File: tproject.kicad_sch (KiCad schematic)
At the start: 28 parts, among them J1 USB_B_Micro, J2 Conn_01x04_Pin, J3 Conn_01x04_Pin, J4 Conn_01x04_Pin, SW1 SW_SPDT, U1 STM32F103C8T6, U2 AMS1117-3.3, Y1 16MHz

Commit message: Replace SW1 with SMD PCM12 footprint, add Wurth USB STEP model, and add design note 0011
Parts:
- SW1: footprint Button_Switch_THT:SW_E-Switch_EG1224_SPDT_Angled -> Button_Switch_SMD:SW_SPDT_PCM12
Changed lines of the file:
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@@
 			)
 		)
-		(property "Footprint" "Button_Switch_THT:SW_E-Switch_EG1224_SPDT_Angled"
+		(property "Footprint" "Button_Switch_SMD:SW_SPDT_PCM12"
 			(at 149.86 62.23 0)
 			(effects

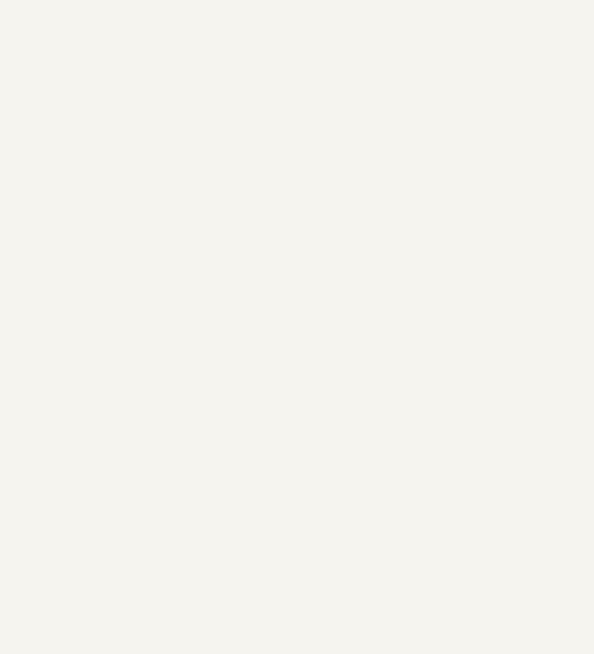
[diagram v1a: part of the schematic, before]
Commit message: Add board outline (38.54x33.17mm), 4x M2 mounting holes, adjust 8 components and add design note 0014
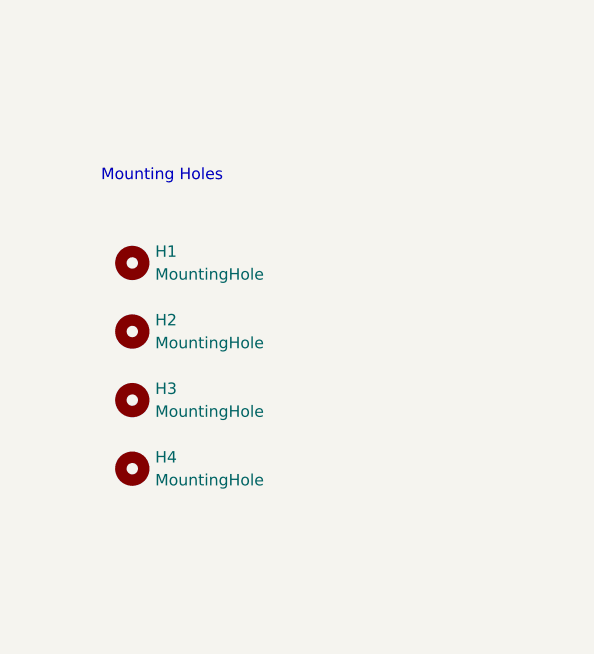
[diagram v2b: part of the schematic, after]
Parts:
- added H1, H2, H3, H4: MountingHole, MountingHole:MountingHole_2.2mm_M2, symbol Mechanical:MountingHole
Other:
- note added: "Mounting Holes"

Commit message: Fix Conn_01x04 footprint: 1.00mm SMD → 2.54mm through-hole (J2, J3, J4)
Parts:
- J2, J3, J4: footprint Connector_PinHeader_1.00mm:PinHeader_1x04_P1.00mm_Vertical_SMD_Pin1Right -> Connector_PinHeader_2.54mm:PinHeader_1x04_P2.54mm_Vertical
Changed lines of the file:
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@@
 			)
 		)
-		(property "Footprint" "Connector_PinHeader_1.00mm:PinHeader_1x04_P1.00mm_Vertical_SMD_Pin1Right"
+		(property "Footprint" "Connector_PinHeader_2.54mm:PinHeader_1x04_P2.54mm_Vertical"
 			(at 236.22 111.76 0)
 			(effects
@@
 			)
 		)
-		(property "Footprint" "Connector_PinHeader_1.00mm:PinHeader_1x04_P1.00mm_Vertical_SMD_Pin1Right"
+		(property "Footprint" "Connector_PinHeader_2.54mm:PinHeader_1x04_P2.54mm_Vertical"
 			(at 124.46 137.16 0)
 			(effects
@@
 			)
 		)
-		(property "Footprint" "Connector_PinHeader_1.00mm:PinHeader_1x04_P1.00mm_Vertical_SMD_Pin1Right"
+		(property "Footprint" "Connector_PinHeader_2.54mm:PinHeader_1x04_P2.54mm_Vertical"
 			(at 124.46 109.22 0)
 			(effects

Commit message: update with prompt result @usb-hub-sch-01-power~
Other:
- added sheet USB Hub (tproject-hub.kicad_sch)
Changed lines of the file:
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@@
+		)
+	)
+	(sheet
+		(at 20 160)
+		(size 30 15)
+		(fields_autoplaced yes)
+		(stroke
+			(width 0.152)
+			(type default)
+		)
+		(fill
+			(color 0 0 0 0.0000)
+		)
+		(property "Sheetname" "USB Hub"
+			(at 20 159.4615 0)
+			(effects
+				(font
+					(size 1.27 1.27)
+					(bold yes)
+				)
+				(justify left)
+			)
+		)
+		(property "Sheetfile" "tproject-hub.kicad_sch"
+			(at 20 175.3846 0)
+			(effects
+				(font
+					(size 1.27 1.27)
+					(italic yes)
+				)
+				(justify left)
+			)
+		)
+		(instances
+			(project "tproject"
+				(path "/6a5b46f1-62dd-49ff-8442-d9907adb115c"
+					(page "2")
+				)
+			)
 		)
 	)
@@
 			(page "1")
 		)
+		(path "/9fc96f67-0000-40fd-835f-e11000000001"
+			(page "2")
+		)
 	)
